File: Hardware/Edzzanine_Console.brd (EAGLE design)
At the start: 30.5 x 44.5 mm, 39 parts, among them U2 FTS31XS-U, U4 TPS62065

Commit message: changes to cap value
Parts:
- C9: value 9.0pF -> 22pF
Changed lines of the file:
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@@
 <element name="R13" library="SparkFun-Resistors" package="0603-RES" value="680k" x="17.78" y="14.732" rot="R90"/>
 <element name="R14" library="SparkFun-Resistors" package="0603-RES" value="120k" x="17.78" y="11.43" rot="R90"/>
-<element name="C9" library="SparkFun-Capacitors" package="0603-CAP" value="9.0pF" x="16.002" y="14.732" rot="R270">
-<attribute name="PROD_ID" value="CAP-09341" x="12.446" y="30.988" size="1.778" layer="27" rot="R270" display="off"/>
+<element name="C9" library="SparkFun-Capacitors" package="0603-CAP" value="22pF" x="16.002" y="14.732" rot="R270">
+<attribute name="PROD_ID" value="CAP-07876" x="12.446" y="30.988" size="1.778" layer="27" rot="R270" display="off"/>
 </element>
 <element name="C10" library="SparkFun-Capacitors" package="0603-CAP" value="4.7uF" x="13.716" y="11.557">

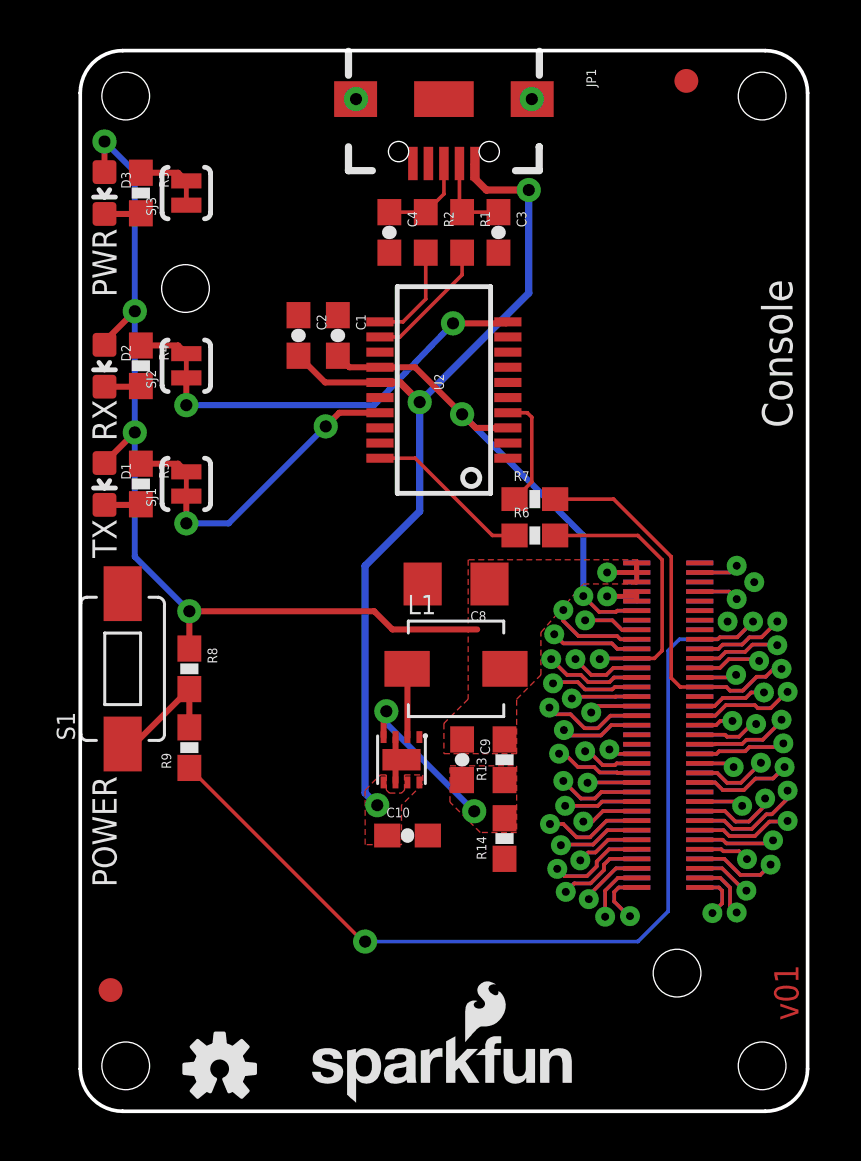
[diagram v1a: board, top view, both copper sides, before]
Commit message: Added DCIN enable circuit replaced power button with new side shooting SMD switch Fixed dimensions corrected ground planes to not include orphans corrected name of board added DCIN pin
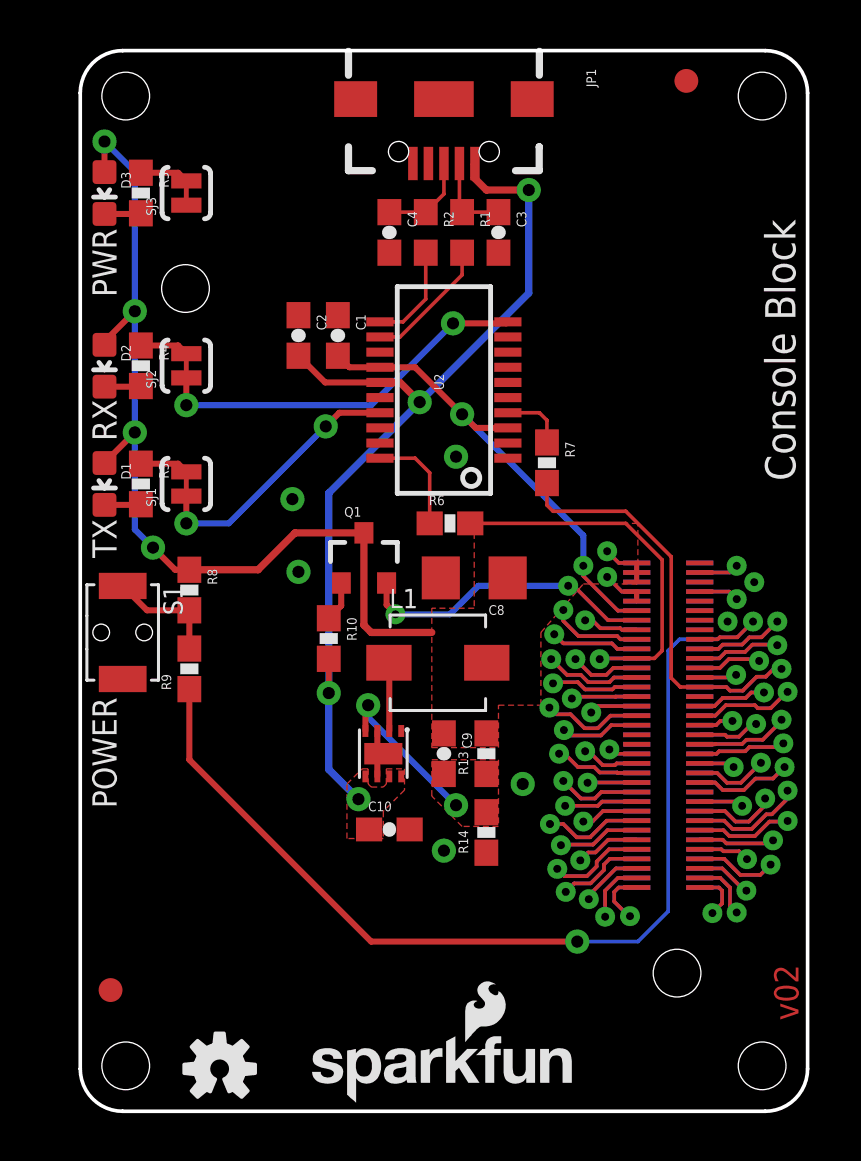
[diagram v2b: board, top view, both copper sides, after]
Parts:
- added Q1: BSS138, SparkFun-DiscreteSemi:SOT23-3
- added R10: 1K, SparkFun-Resistors:0603-RES
- S1: device SparkFun-Electromechanical:TACTILE-SWITCH-1101NE -> SparkFun-Electromechanical:TACTILE_SWITCH-SMD-RIGHT-ANGLE
- moved R6 3.59 mm to (15.5, 24.6)
- moved R9 3.30 mm to (4.57, 18.5)
- moved R8 3.30 mm to (4.57, 21.8)
- moved R7 1.61 mm to (19.6, 27.2), turned to 270 degrees
- moved S1 1.52 mm to (1.78, 20.1), turned to 270 degrees
- moved C8 0.80 mm to (16.5, 22.4)
- moved R13 0.80 mm to (17.0, 15.0)
- moved U4 0.80 mm to (12.7, 15.0)
- moved R14 0.80 mm to (17.0, 11.7)
- moved C9 0.80 mm to (15.2, 15.0)
- moved C10 0.80 mm to (13.0, 11.8)
- moved L1 0.80 mm to (15.0, 18.8)
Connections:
- new net DCIN: E1.14, Q1.2, U$3.14
- new net N$16: Q1.1, R10.1
- net 5V: now also R10.2
- net GND: now also S1.2; no longer S1.P$2
- net N$15: now also S1.1; no longer S1.P$1
- net VSYS: now also Q1.3
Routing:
- net DCIN: track 0.00 -> 16.1 mm, vias 0 -> 2
- net GP134_UART_2_RX: track 13.0 -> 16.8 mm
- net PWRBTN#: track 41.1 -> 44.2 mm
- net N$11: track 6.98 -> 4.46 mm
- net 5V: track 37.8 -> 39.9 mm, vias 3 -> 4
- net N$14: track 4.81 -> 2.70 mm
- net N$16: track 0.00 -> 1.69 mm
- net GP135_UART_2_TX: track 20.0 -> 21.2 mm
- net N$15: track 5.35 -> 4.82 mm
- net GND: vias 4 -> 7
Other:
- board text added: "Console Block"
- board text added: "NOTE: Units are in Inches"
- board text added: "v02"
- board text removed: "Connectors Go Here"
- board text removed: "Console"
- board text removed: "LED's and selector switches go here"
- board text removed: "Max Board Length"
- board text removed: "Nothing goes here... I mean it."
- board text removed: "v01"
